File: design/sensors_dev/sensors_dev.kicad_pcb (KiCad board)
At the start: 2 copper layers, 46 parts, among them J1 Conn_01x02, J2 Conn_01x15, J3 Conn_01x15, J4 Conn_01x12, Q1 RE1C002UN, Q2 RE1C002UN, U1 LP2980AIM5-3.0, U2 BMC150, U3 LSM6DS3HTR, U4 BMG250, U5 MS5607-02BA03, U6 LIS3DHTR

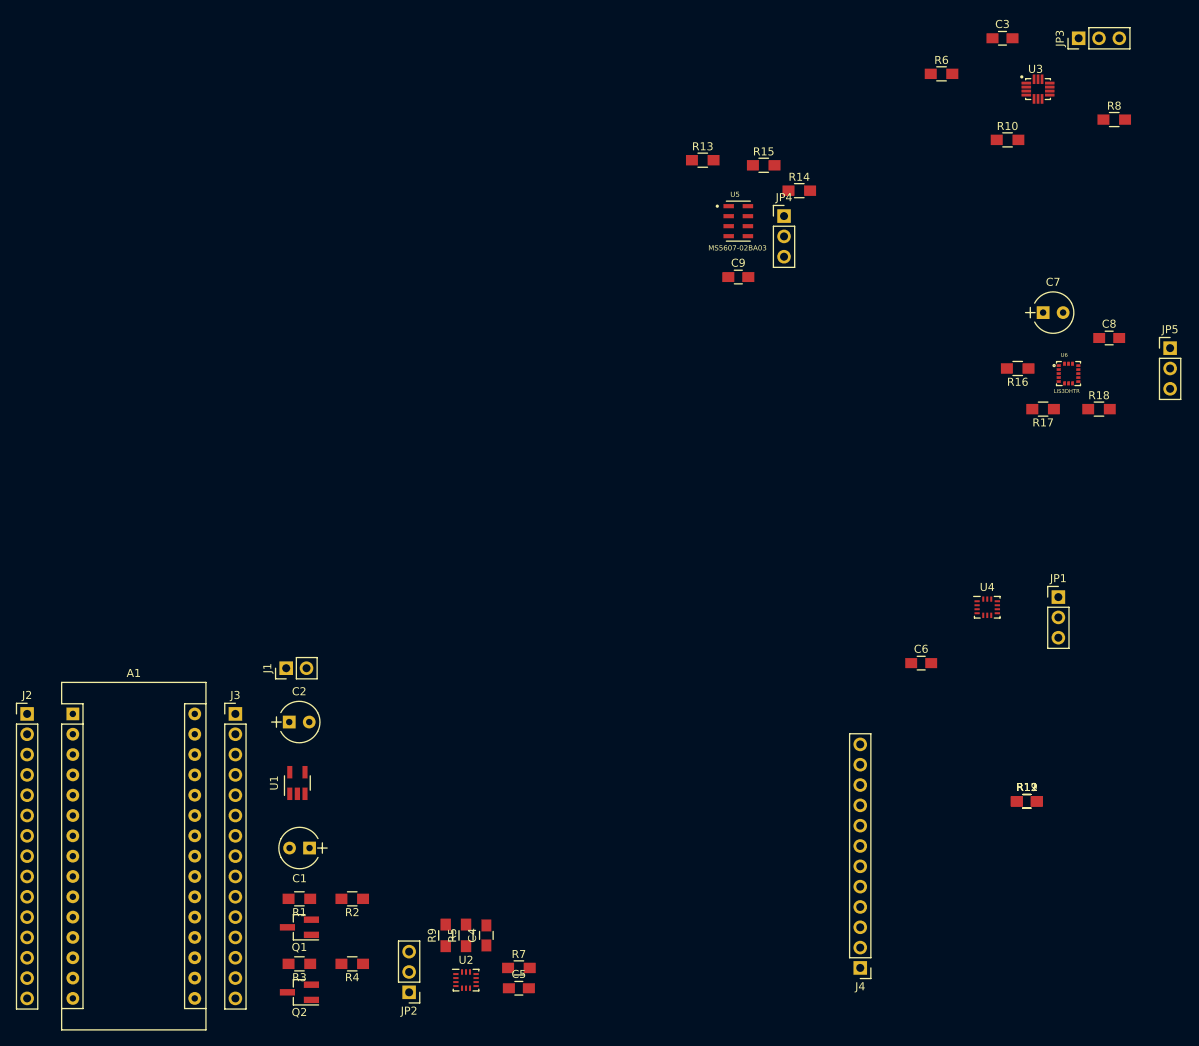
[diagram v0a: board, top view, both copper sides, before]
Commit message: First draft PCB layout
Todo: move arduino off board (use a breadboard instead). Will save a lot
of space on the PCB and make the prototype cheaper.
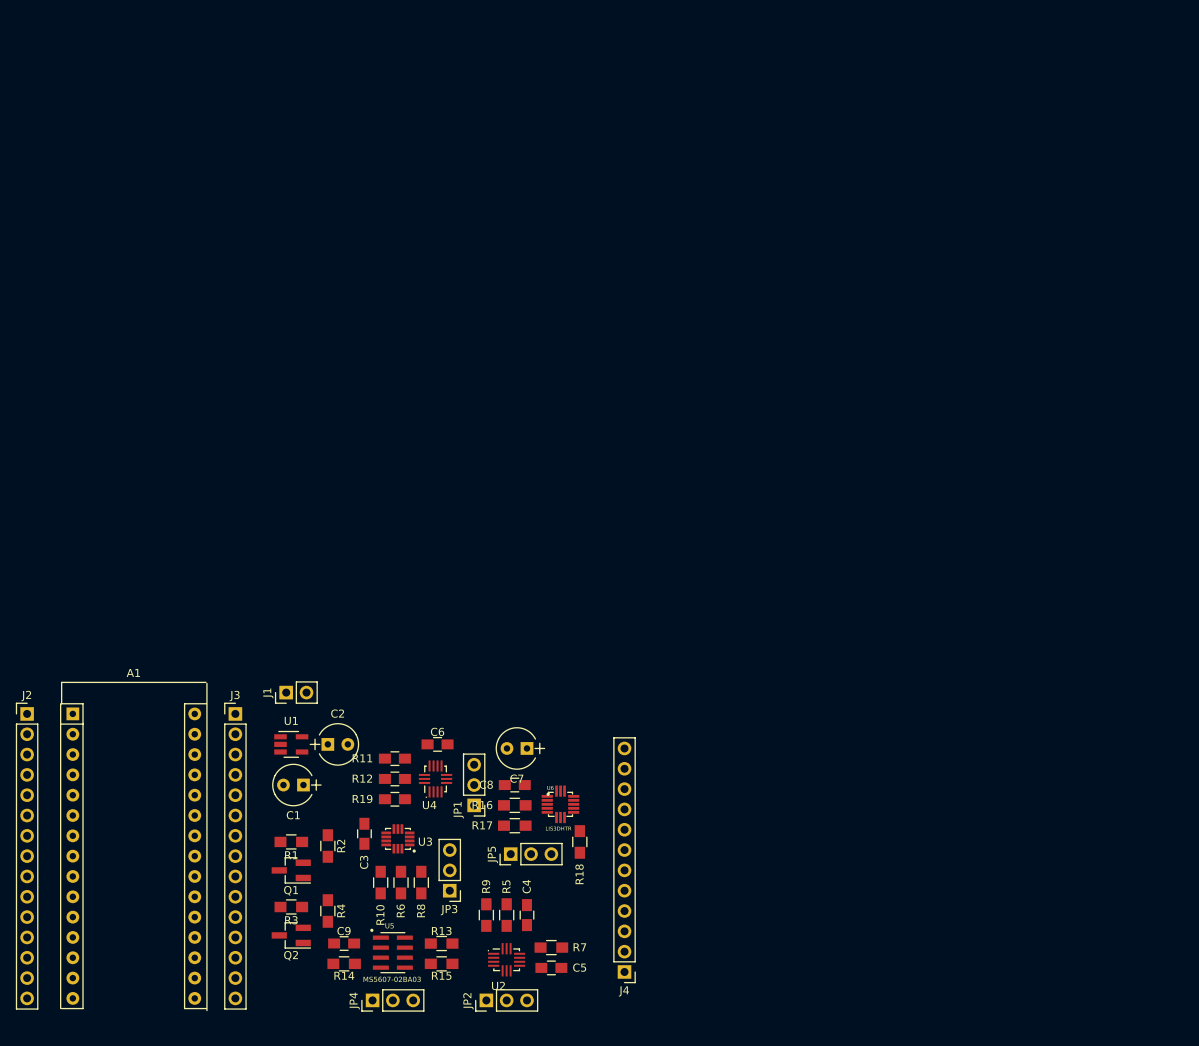
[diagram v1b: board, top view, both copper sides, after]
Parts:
- U2, U4: footprint Package_LGA:Bosch_LGA-14_3x2.5mm_P0.5mm -> footprints:Bosch_LGA-14
- U5: footprint MS560702BA03-50:SON125P300X500X100-8N -> footprints:MS560702BA03
- U6: footprint LIS3DHTR:LGA16R50P5X3_300X300X100N -> footprints:LGA16_LIS3DHTR
- moved JP3 132.4 mm to (126.5, 137.7), turned to 180 degrees
- moved R8 128.8 mm to (122.9, 136.7), turned to 270 degrees
- moved C3 127.5 mm to (115.8, 130.6), turned to 270 degrees
- moved U3 123.2 mm to (120.0, 131.2), turned to 180 degrees
- moved R6 121.6 mm to (120.4, 136.7), turned to 270 degrees
- moved R10 121.5 mm to (117.9, 136.7), turned to 270 degrees
- moved R14 112.2 mm to (113.3, 146.8), turned to 180 degrees
- moved JP4 110.7 mm to (116.8, 151.4), turned to 90 degrees
- moved R15 107.6 mm to (125.5, 146.8), turned to 180 degrees
- moved JP5 103.9 mm to (134.1, 133.1), turned to 90 degrees
- moved R13 103.2 mm to (125.5, 144.3)
- moved U5 101.1 mm to (119.4, 145.4)
- moved C9 96.8 mm to (113.3, 144.3), turned to 180 degrees
- moved C8 93.0 mm to (134.6, 124.5), turned to 180 degrees
- moved R18 84.5 mm to (142.7, 131.6), turned to 270 degrees
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
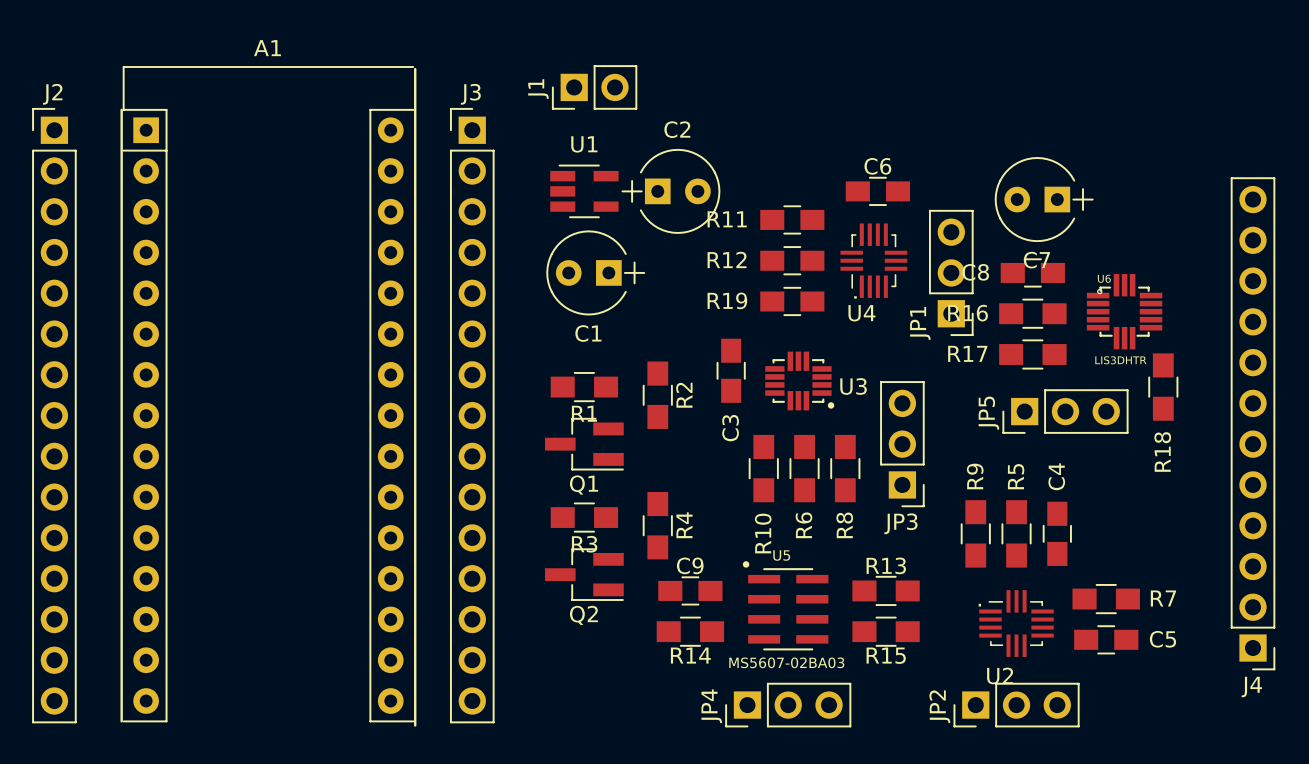
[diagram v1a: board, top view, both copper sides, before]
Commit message: First pass board routing.
Also, remove arduino from PCB since this is a dev board and there's no
point paying for extra unused board space.
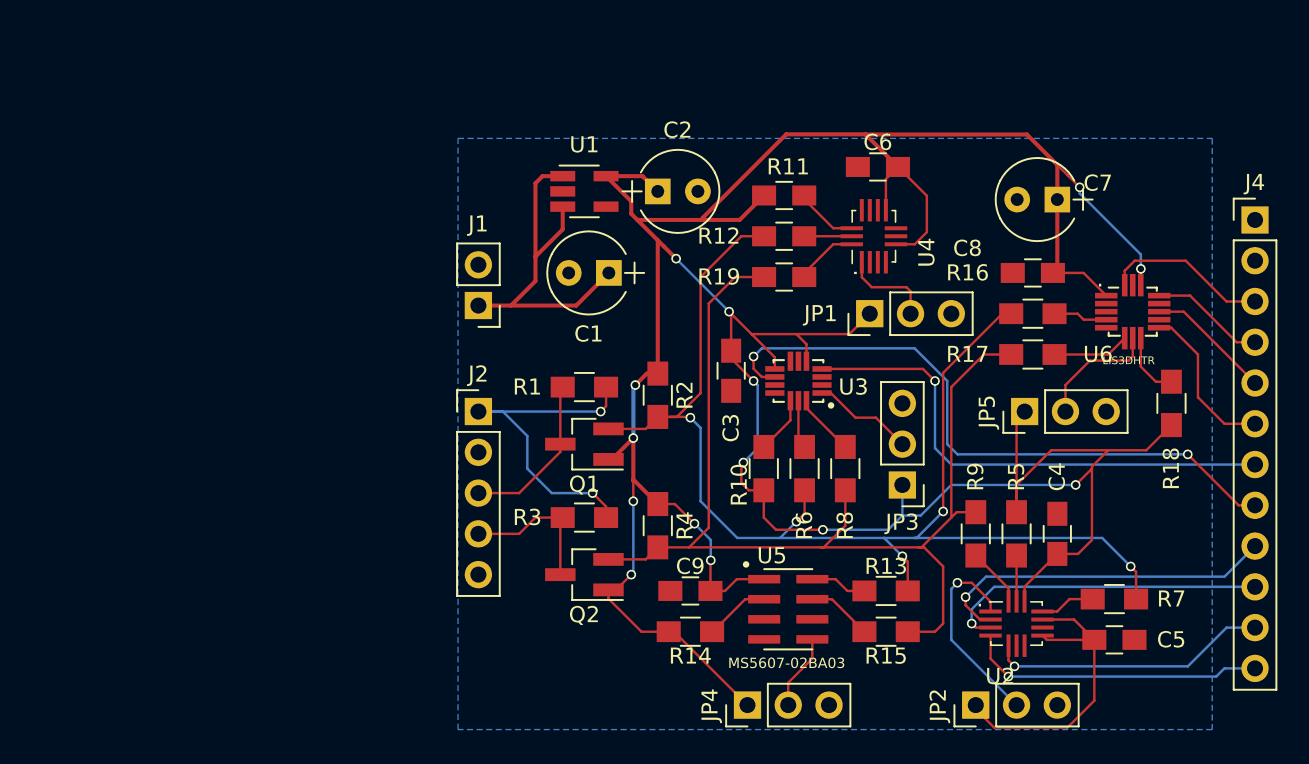
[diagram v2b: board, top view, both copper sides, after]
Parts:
- removed A1: Arduino_Nano_v3.x, Module:Arduino_Nano
- removed J3: Conn_01x15, Pin_Headers:Pin_Header_Straight_1x15_Pitch2.54mm
- J2: value Conn_01x15 -> Conn_01x05; footprint Pin_Headers:Pin_Header_Straight_1x15_Pitch2.54mm -> Pin_Headers:Pin_Header_Straight_1x05_Pitch2.54mm
- U6: footprint footprints:LGA16_LIS3DHTR -> LGA16_LIS3DHTR
- moved J2 31.7 mm to (100.1, 133.1)
- moved J4 26.7 mm to (148.5, 121.2), turned to 0 degrees
- moved J1 14.8 mm to (100.1, 126.5), turned to 180 degrees
- moved JP1 5.08 mm to (124.5, 127.0), turned to 90 degrees
- moved R11 1.61 mm to (119.1, 119.6)
- moved R19 1.61 mm to (119.1, 124.7)
- moved R12 1.61 mm to (119.1, 122.2)
- moved C6 1.52 mm to (125.0, 117.9)
- moved U4 1.52 mm to (124.7, 122.2)
- moved R18 1.14 mm to (143.3, 132.6)
- moved C5 0.51 mm to (139.7, 147.3)
- moved R7 0.51 mm to (139.7, 144.8)
- moved U6 0.51 mm to (140.8, 126.9)
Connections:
- J2 pad 1: Net-(A1-Pad1) -> +5V
- J2 pad 2: Net-(A1-Pad2) -> +7.5V
- J2 pad 3: Net-(A1-Pad3) -> /SCL_5V
- J2 pad 4: GND -> /SDA_5V
- J2 pad 5: Net-(A1-Pad5) -> GND
- J4 pad 1: /Eval Sensors/GYRO_INT1 -> /Eval Sensors/GYRO_INT2
- J4 pad 2: /Eval Sensors/GYRO_INT2 -> /Eval Sensors/GYRO_INT1
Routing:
- net +3.0V: track 0.00 -> 238.8 mm, vias 0 -> 14
- net SCL_3V: track 0.00 -> 80.7 mm, vias 0 -> 5
- net SDA_3V: track 0.00 -> 68.9 mm
- net /Eval Sensors/IMU_INT2: track 0.00 -> 40.1 mm, vias 0 -> 2
- net /Eval Sensors/IMU_INT1: track 0.00 -> 31.9 mm, vias 0 -> 1
- net +7.5V: track 0.00 -> 22.9 mm
- net /Eval Sensors/MAG_INT1: track 0.00 -> 21.8 mm, vias 0 -> 1
- net +5V: track 0.00 -> 21.6 mm, vias 0 -> 2
- net /Eval Sensors/MAG_INT2: track 0.00 -> 20.4 mm, vias 0 -> 1
- net /Eval Sensors/MAG_DRDY: track 0.00 -> 18.6 mm, vias 0 -> 1
- net /Eval Sensors/MAG_INT3: track 0.00 -> 17.4 mm, vias 0 -> 1
- net Net-(JP2-Pad2): track 0.00 -> 12.6 mm, vias 0 -> 1
- net /Eval Sensors/ACC_ADC1: track 0.00 -> 10.3 mm
- net /SCL_5V: track 0.00 -> 10.3 mm
- net /Eval Sensors/ACC_INT2: track 0.00 -> 10.0 mm
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- added copper zone on B.Cu, net GND

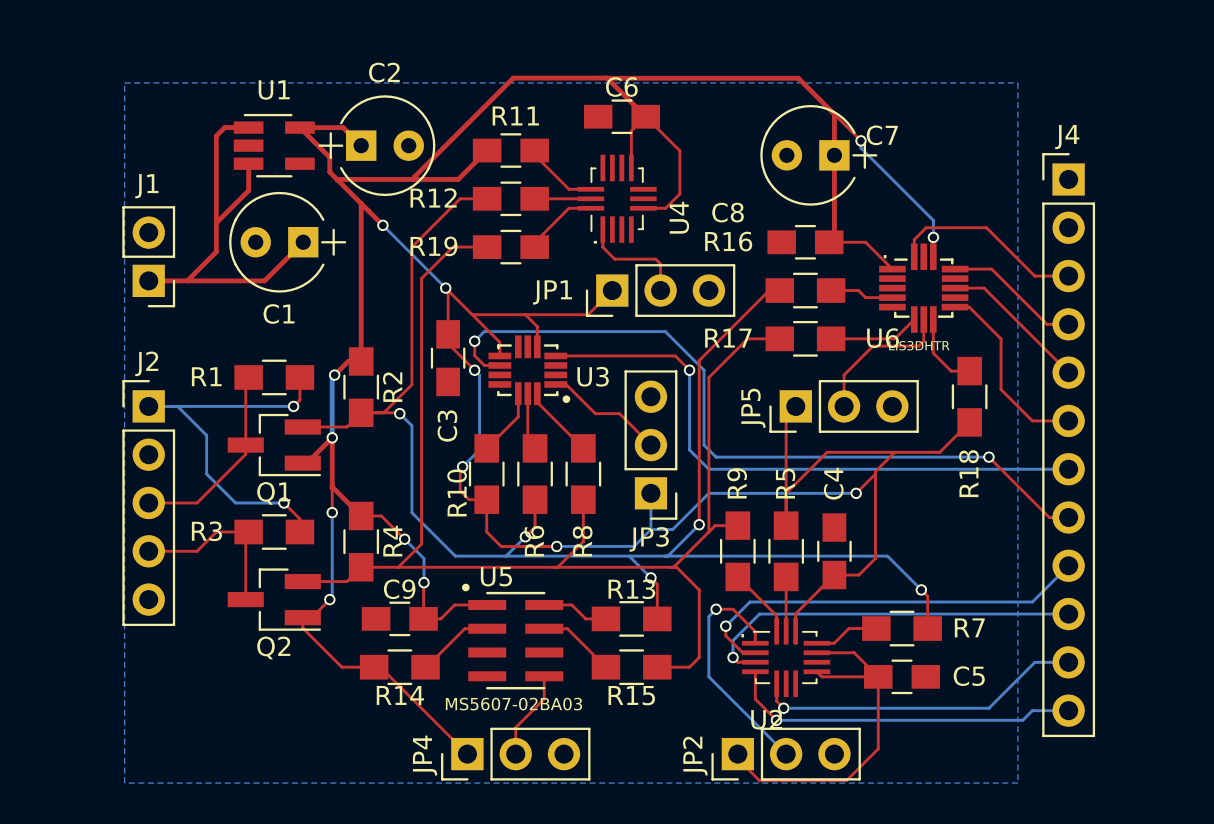
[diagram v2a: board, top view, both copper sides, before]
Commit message: Redo board placement and routing
Will send to fab after final review.
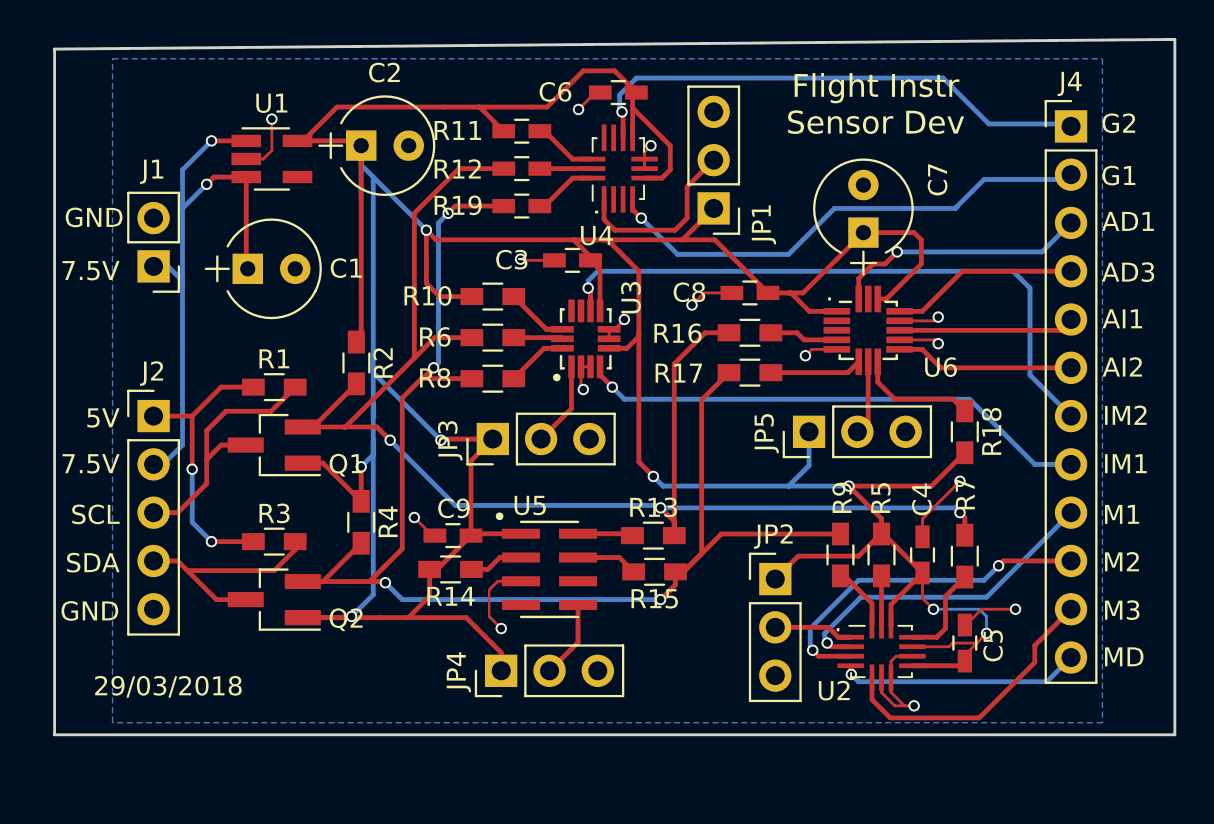
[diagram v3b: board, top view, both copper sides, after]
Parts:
- C3, C4, C5, C6, C8, C9, R11, R12, R19: footprint Capacitors_SMD:C_0805_HandSoldering -> Capacitors_SMD:C_0603_HandSoldering
- R1, R10, R13, R14, R15, R16, R17, R18, R2, R3, R4, R5, R6, R7, R8, R9: footprint Resistors_SMD:R_0805_HandSoldering -> Resistors_SMD:R_0603_HandSoldering
- U6: footprint LGA16_LIS3DHTR -> footprints:LGA16_LIS3DHTR
- moved JP2 9.42 mm to (133.0, 142.2), turned to 0 degrees
- moved R10 9.34 mm to (118.2, 127.3), turned to 180 degrees
- moved JP3 8.80 mm to (118.2, 134.8), turned to 90 degrees
- moved C3 8.32 mm to (122.4, 125.4), turned to 180 degrees
- moved R6 7.51 mm to (118.2, 129.5), turned to 180 degrees
- moved R8 6.92 mm to (118.2, 131.6), turned to 180 degrees
- moved JP1 6.86 mm to (129.8, 122.7), turned to 180 degrees
- moved R14 5.79 mm to (116.0, 141.7)
- moved R9 5.40 mm to (136.5, 140.9)
- moved C9 5.20 mm to (116.1, 139.9)
- moved R15 5.16 mm to (126.7, 141.8)
- moved R7 5.04 mm to (143.0, 141.0), turned to 90 degrees
- moved U2 5.03 mm to (138.6, 146.0)
- moved R5 5.02 mm to (138.6, 140.9)
- moved JP4 4.73 mm to (118.6, 147.0)
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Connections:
- J4 pad 7: /Eval Sensors/IMU_INT1 -> /Eval Sensors/IMU_INT2
- J4 pad 8: /Eval Sensors/IMU_INT2 -> /Eval Sensors/IMU_INT1
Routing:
- net GND: track 0.00 -> 38.5 mm, vias 0 -> 15
- net /Eval Sensors/GYRO_INT2: track 0.00 -> 27.5 mm, vias 0 -> 1
- net /Eval Sensors/GYRO_INT1: track 0.00 -> 26.5 mm, vias 0 -> 1
- net +7.5V: track 22.9 -> 31.4 mm, vias 0 -> 2
- net Net-(JP2-Pad2): track 12.6 -> 4.71 mm, vias 1 -> 0
- net /Eval Sensors/IMU_INT2: track 40.1 -> 33.1 mm, vias 2 -> 1
- net +5V: track 21.6 -> 15.1 mm
- net /Eval Sensors/MAG_DRDY: track 18.6 -> 12.7 mm
- net /Eval Sensors/IMU_INT1: track 31.9 -> 27.2 mm
- net /Eval Sensors/MAG_INT1: track 21.8 -> 17.5 mm
- net /SCL_5V: track 10.3 -> 14.2 mm
- net Net-(JP1-Pad2): track 5.73 -> 9.55 mm
- net Net-(JP5-Pad2): track 7.72 -> 3.92 mm
- net /Eval Sensors/ACC_ADC1: track 10.3 -> 13.6 mm, vias 0 -> 1
- net /SDA_5V: track 9.29 -> 12.2 mm
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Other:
- board outline added: 58.9 x 36.6 mm
- board text added: "29/03/2018"
- board text added: "5V"
- board text added: "7.5V"
- board text added: "AD1"
- board text added: "AD3"
- board text added: "AI1"
- board text added: "AI2"
- board text added: "Flight Instr Sensor Dev"
- board text added: "G1"
- board text added: "G2"
- board text added: "GND"
- board text added: "IM1"
- board text added: "IM2"
- board text added: "M1"
- board text added: "M2"
- board text added: "M3"
- board text added: "MD"
- board text added: "SCL"
- board text added: "SDA"
